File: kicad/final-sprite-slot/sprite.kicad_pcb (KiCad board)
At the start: 4 copper layers, 35 x 44.6 mm, 66 parts, among them J1 M20-7910442R, U1 CC430F513X, U2 LSM9DS1, U3 SPRITETCXO_TCXO_7Z, U4 DRV8837, U5 ADP5092, U6 DRV8837, U7 DRV8837, X1 SPRITEPIN_SPRITE_PIN, X2 SPRITEPIN_SPRITE_PIN

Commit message: Remove back silkscreen logo
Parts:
- removed the G*** at (149.6, 96.0)

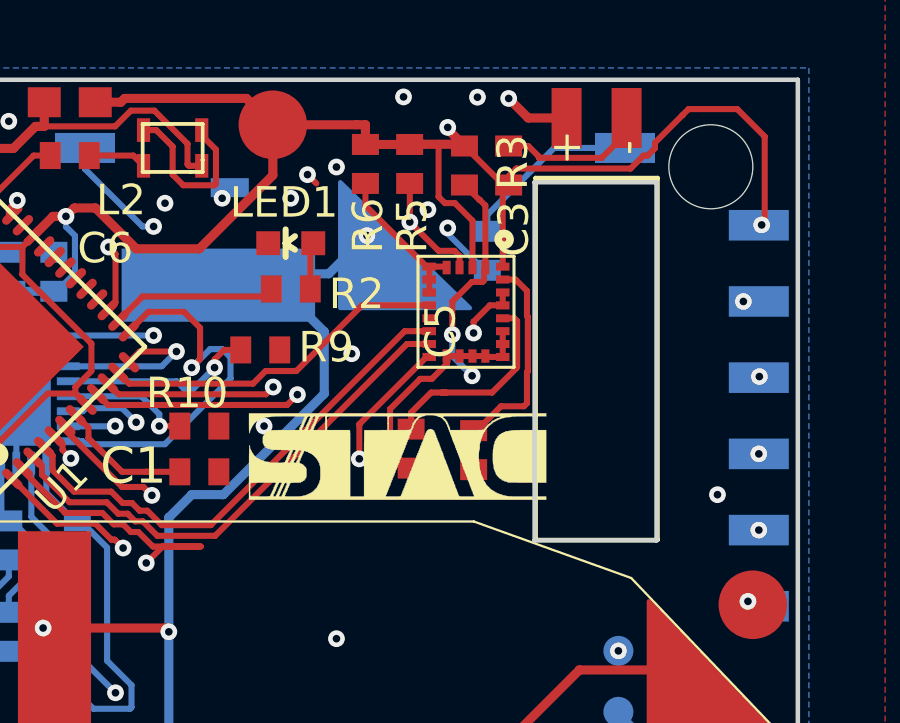
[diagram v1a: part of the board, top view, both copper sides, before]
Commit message: Add more slot margin and move top logo
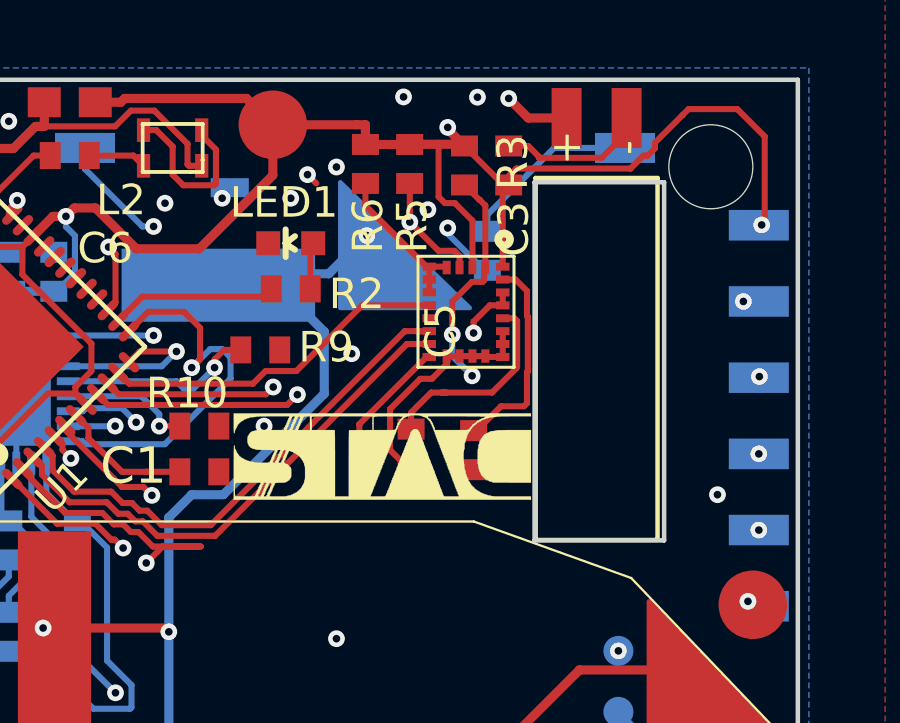
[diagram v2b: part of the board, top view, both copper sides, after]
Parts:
- moved G*** 0.51 mm to (142.0, 96.0)
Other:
- outline, holes or cut-outs redrawn
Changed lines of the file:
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@@
     (38 B.Mask user)
     (39 F.Mask user)
-    (40 Dwgs.User user hide)
-    (41 Cmts.User user hide)
-    (42 Eco1.User user hide)
-    (43 Eco2.User user hide)
+    (40 Dwgs.User user)
+    (41 Cmts.User user)
+    (42 Eco1.User user)
+    (43 Eco2.User user)
     (44 Edge.Cuts user)
-    (45 Margin user hide)
+    (45 Margin user)
     (46 B.CrtYd user)
     (47 F.CrtYd user)
-    (48 B.Fab user hide)
-    (49 F.Fab user hide)
+    (48 B.Fab user)
+    (49 F.Fab user)
   )
   (setup
@@
   )
   (module sprite:logo locked (layer Top)
-    (at 142.494 96.012)
+    (at 141.986 96.012)
     (fp_text reference G*** (at 0 0) (layer F.SilkS) hide
       (effects (font (size 1.524 1.524) (thickness 0.3)))
@@
   )
   (gr_line (start 147.066 98.806) (end 147.066 86.868) (layer Edge.Cuts) (width 0.15))
-  (gr_line (start 151.13 98.806) (end 147.066 98.806) (layer Edge.Cuts) (width 0.15))
-  (gr_line (start 151.13 86.868) (end 151.13 98.806) (layer Edge.Cuts) (width 0.15))
-  (gr_line (start 147.066 86.868) (end 151.13 86.868) (layer Edge.Cuts) (width 0.15))
+  (gr_line (start 151.384 98.806) (end 147.066 98.806) (layer Edge.Cuts) (width 0.15))
+  (gr_line (start 151.384 86.868) (end 151.384 98.806) (layer Edge.Cuts) (width 0.15))
+  (gr_line (start 147.066 86.868) (end 151.384 86.868) (layer Edge.Cuts) (width 0.15))
   (gr_text "STAC Spinor in Space!" (at 135.89 122.428 198) (layer B.SilkS)
     (effects (font (size 1.5 1.5) (thickness 0.3)) (justify mirror))
@@
       )
     )
-  )
-  (zone (net 0) (net_name "") (layers Top Route2 Route3 Bottom) (hatch edge 0.508)
-    (connect_pads (clearance 0.2794))
-    (min_thickness 0.254)
-    (keepout (tracks not_allowed) (vias not_allowed) (copperpour allowed))
-    (fill (arc_segments 16) (thermal_gap 0.508) (thermal_bridge_width 0.508))
-    (polygon
-      (pts
-        (xy 146.9136 86.7156) (xy 151.2316 86.7156) (xy 151.2824 99.0092) (xy 146.9644 98.8568) (xy 146.9136 92.202)
-        (xy 146.9136 86.7664)
-      )
-    )

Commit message: Fix unconnected
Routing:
- net Net-(R6-Pad2): track 26.4 -> 16.3 mm
- net GND: vias 26 -> 29

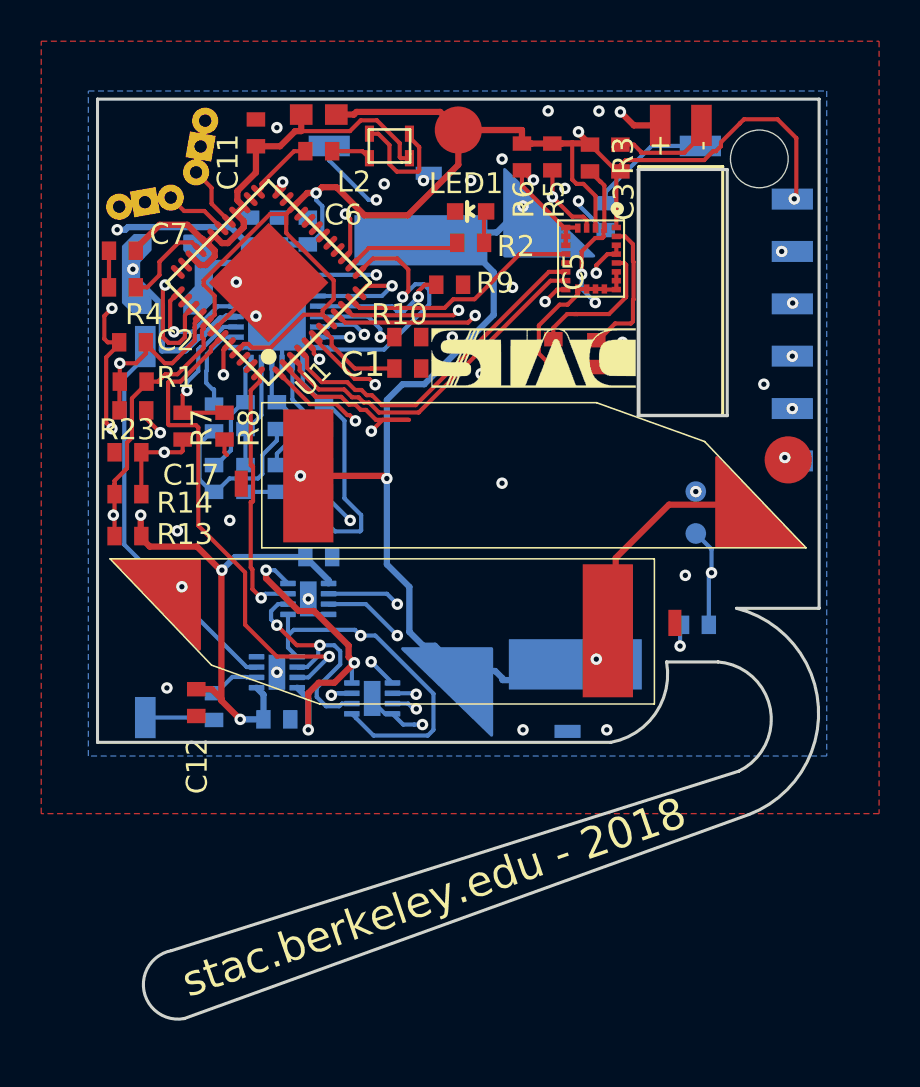
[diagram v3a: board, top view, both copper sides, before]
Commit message: Flip UMAC connectors and offset coil pad
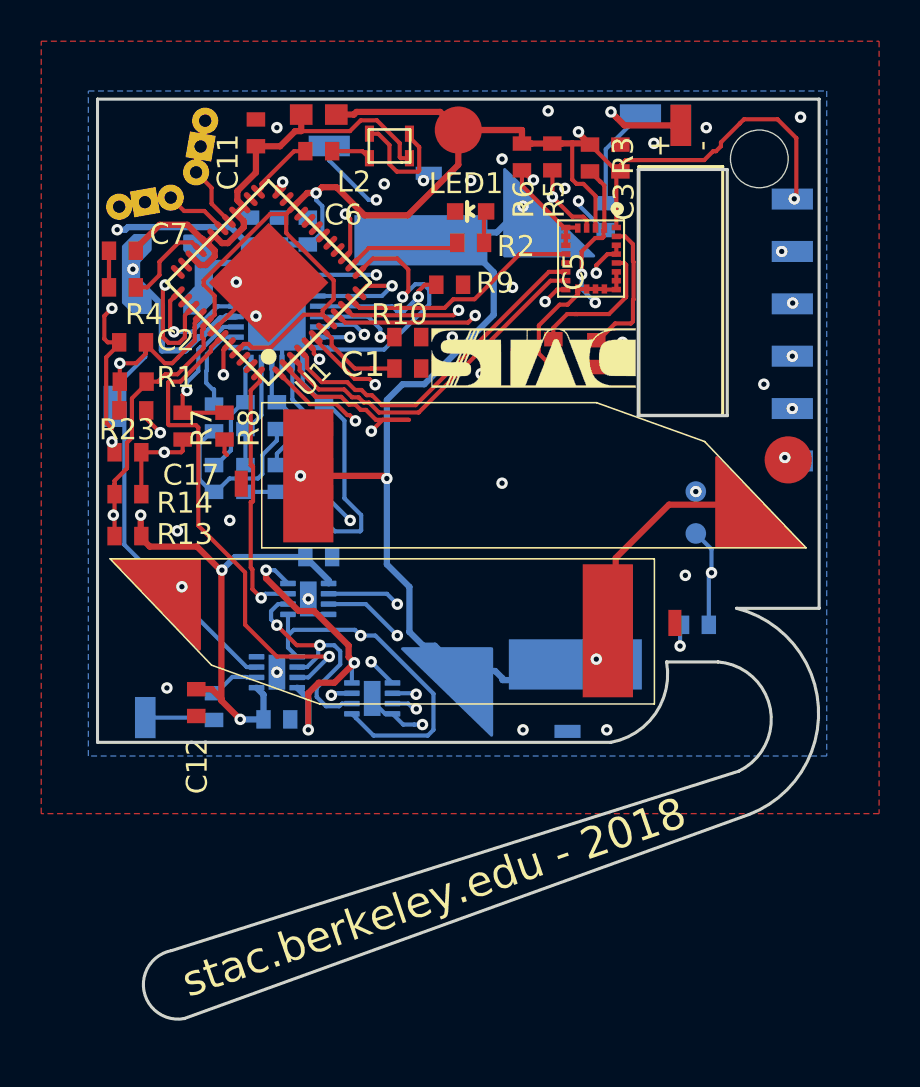
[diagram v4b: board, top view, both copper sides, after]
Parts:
- B1: value UMAC_UMAC -> UMAC_TWOSIDE; footprint sprite:UMAC_UMAC -> sprite:UMAC_TWOSIDE
- L3, L4: value PCBSAT-TORQUECOIL -> PCBSAT-TORQUECOIL-OFFSET; footprint sprite:PCBSAT-TORQUECOIL -> sprite:PCBSAT-TORQUECOIL-OFFSET
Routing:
- net GND: track 51.3 -> 46.4 mm, vias 29 -> 31
- net Net-(L4-Pad1): track 6.06 -> 5.00 mm
- net /VBAT: track 22.3 -> 23.3 mm
- net Net-(L3-Pad1): track 18.9 -> 19.4 mm
